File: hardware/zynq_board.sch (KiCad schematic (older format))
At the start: 0 parts

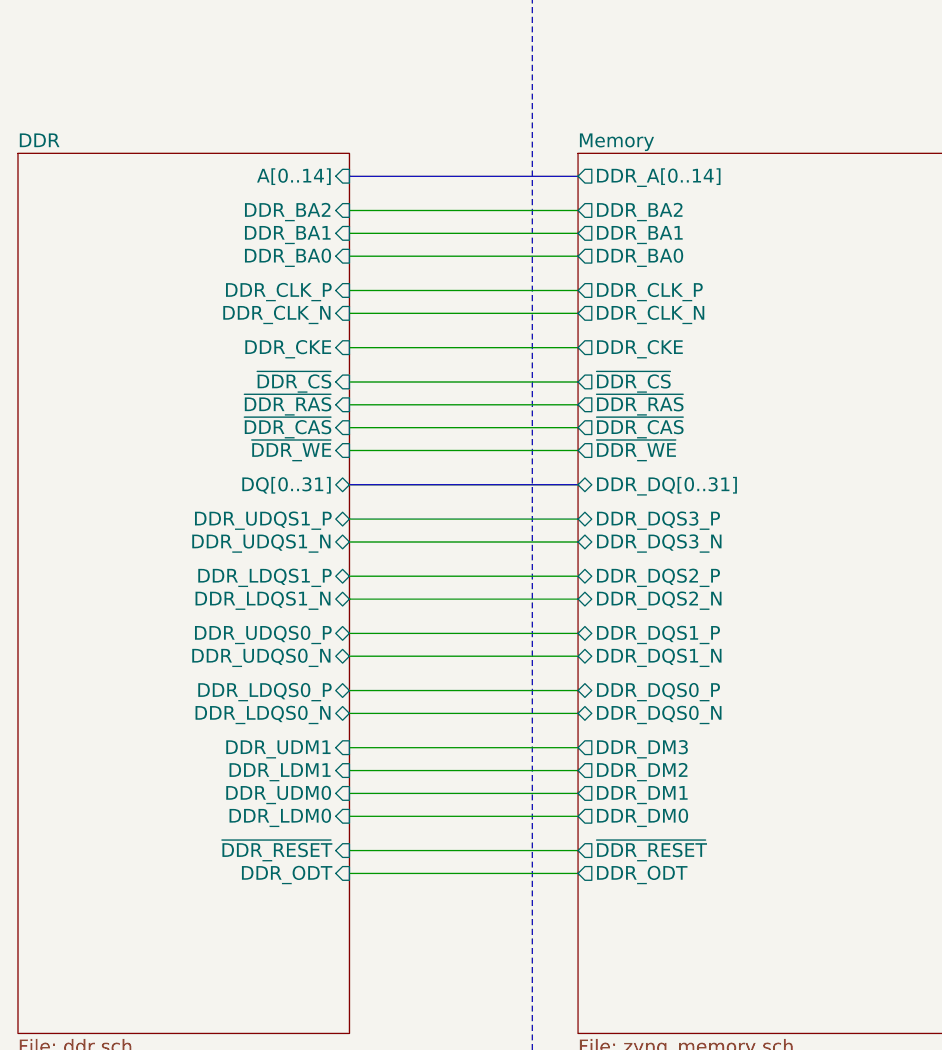
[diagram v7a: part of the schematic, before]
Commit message: Moved the FPGAs Memory Port to the DDR Sheet due KiCad 4.0.7 does not support Busses through hiearchical Labels
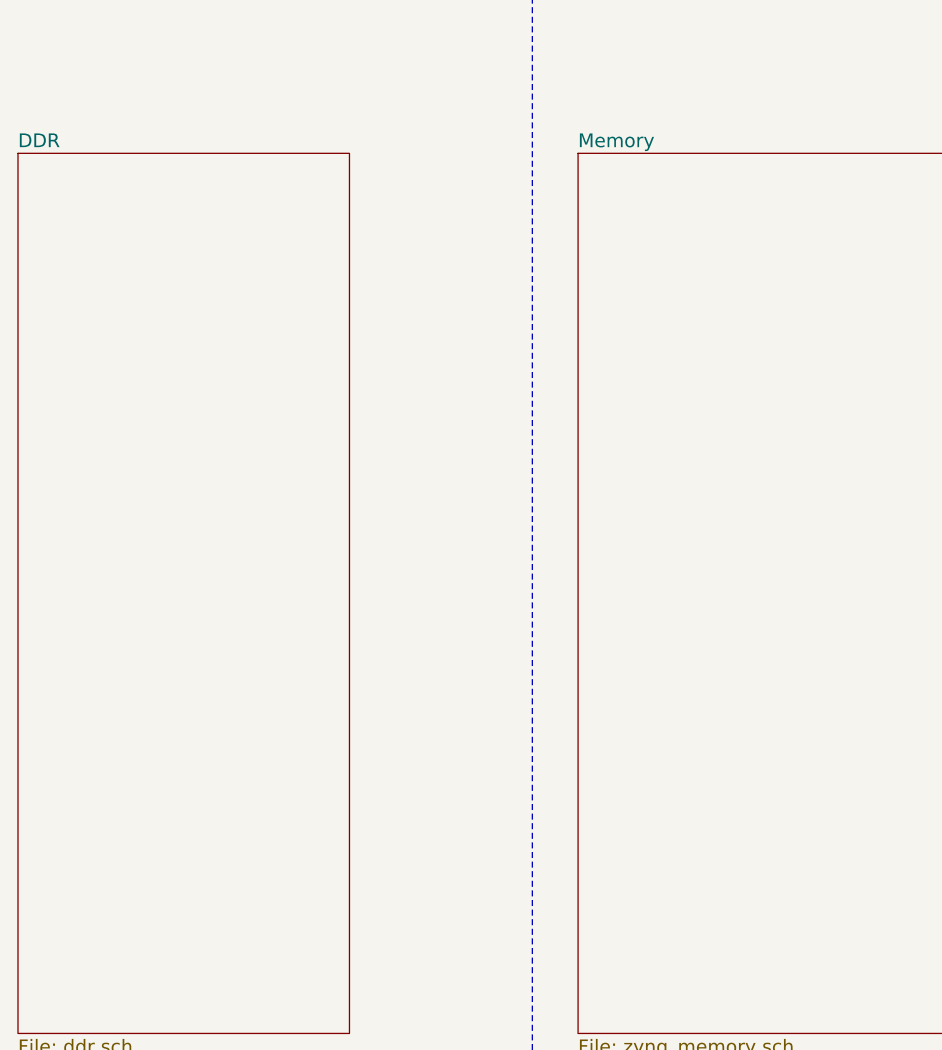
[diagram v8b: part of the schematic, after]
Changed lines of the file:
@@
 F0 "Memory" 60
 F1 "zynq_memory.sch" 60
-F2 "DDR_BA0" O L 7450 16350 60
-F3 "DDR_BA1" O L 7450 16250 60
-F4 "DDR_BA2" O L 7450 16150 60
-F5 "DDR_CKE" O L 7450 16750 60
-F6 "DDR_CLK_N" O L 7450 16600 60
-F7 "DDR_CLK_P" O L 7450 16500 60
-F8 "DDR_DM0" O L 7450 18800 60
-F9 "DDR_DM1" O L 7450 18700 60
-F10 "DDR_DM2" O L 7450 18600 60
-F11 "DDR_DM3" O L 7450 18500 60
-F12 "DDR_DQS0_N" B L 7450 18350 60
-F13 "DDR_DQS1_N" B L 7450 18100 60
-F14 "DDR_DQS2_N" B L 7450 17850 60
-F15 "DDR_DQS3_N" B L 7450 17600 60
-F16 "DDR_DQS0_P" B L 7450 18250 60
-F17 "DDR_DQS1_P" B L 7450 18000 60
-F18 "DDR_DQS2_P" B L 7450 17750 60
-F19 "DDR_DQS3_P" B L 7450 17500 60
-F20 "DDR_ODT" O L 7450 19050 60
-F21 "DDR_A[0..14]" O L 7450 16000 60
-F22 "DDR_DQ[0..31]" B L 7450 17350 60
-F23 "~DDR_CAS~" O L 7450 17100 60
-F24 "~DDR_CS~" O L 7450 16900 60
-F25 "~DDR_RESET~" O L 7450 18950 60
-F26 "~DDR_RAS~" O L 7450 17000 60
-F27 "~DDR_WE~" O L 7450 17200 60
 $EndSheet
 $Sheet
@@
 F0 "DDR" 60
 F1 "ddr.sch" 60
-F2 "DDR_LDQS0_P" B R 6450 18250 60
-F3 "DDR_LDQS0_N" B R 6450 18350 60
-F4 "DDR_UDQS0_P" B R 6450 18000 60
-F5 "DDR_UDQS0_N" B R 6450 18100 60
-F6 "DDR_ODT" I R 6450 19050 60
-F7 "DDR_BA2" I R 6450 16150 60
-F8 "DDR_BA1" I R 6450 16250 60
-F9 "DDR_BA0" I R 6450 16350 60
-F10 "DDR_CKE" I R 6450 16750 60
-F11 "DDR_CLK_P" I R 6450 16500 60
-F12 "DDR_CLK_N" I R 6450 16600 60
-F13 "DDR_UDM0" I R 6450 18700 60
-F14 "DDR_LDM0" I R 6450 18800 60
-F15 "DQ[0..31]" B R 6450 17350 60
-F16 "DDR_LDQS1_P" B R 6450 17750 60
-F17 "DDR_LDQS1_N" B R 6450 17850 60
-F18 "DDR_UDQS1_P" B R 6450 17500 60
-F19 "DDR_UDQS1_N" B R 6450 17600 60
-F20 "DDR_UDM1" I R 6450 18500 60
-F21 "DDR_LDM1" I R 6450 18600 60
-F22 "A[0..14]" I R 6450 16000 60
-F23 "~DDR_RESET~" I R 6450 18950 60
-F24 "~DDR_CAS~" I R 6450 17100 60
-F25 "~DDR_RAS~" I R 6450 17000 60
-F26 "~DDR_CS~" I R 6450 16900 60
-F27 "~DDR_WE~" I R 6450 17200 60
 $EndSheet
 $Sheet
@@
 Wire Wire Line
 	13250 18250 20600 18250
-Wire Bus Line
-	6450 16000 7450 16000
-Wire Wire Line
-	6450 16150 7450 16150
-Wire Wire Line
-	6450 16250 7450 16250
-Wire Wire Line
-	6450 16350 7450 16350
-Wire Wire Line
-	6450 16500 7450 16500
-Wire Wire Line
-	7450 16600 6450 16600
-Wire Wire Line
-	6450 16750 7450 16750
-Wire Bus Line
-	6450 17350 7450 17350
-Wire Wire Line
-	6450 17500 7450 17500
-Wire Wire Line
-	7450 17600 6450 17600
-Wire Wire Line
-	6450 17750 7450 17750
-Wire Wire Line
-	7450 17850 6450 17850
-Wire Wire Line
-	6450 18000 7450 18000
-Wire Wire Line
-	7450 18100 6450 18100
-Wire Wire Line
-	6450 18250 7450 18250
-Wire Wire Line
-	7450 18350 6450 18350
-Wire Wire Line
-	6450 18500 7450 18500
-Wire Wire Line
-	7450 18600 6450 18600
-Wire Wire Line
-	6450 18700 7450 18700
-Wire Wire Line
-	7450 18800 6450 18800
-Wire Wire Line
-	6450 18950 7450 18950
-Wire Wire Line
-	7450 19050 6450 19050
-Wire Wire Line
-	6450 16900 7450 16900
-Wire Wire Line
-	7450 17000 6450 17000
-Wire Wire Line
-	6450 17100 7450 17100
-Wire Wire Line
-	7450 17200 6450 17200
 Wire Wire Line
 	6500 8550 7450 8550
